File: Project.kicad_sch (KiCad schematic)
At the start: 76 parts, among them J1 Screw_Terminal_01x02, J2 Screw_Terminal_01x02, J3 Conn_01x04_Socket, Q1 BT136-500, SW1 PEC11H, SW2 PEC11H, U1 AMS1117-3.3, U2 ESP32-WROOM-32, U3 MOC3021M, U4 MCT2E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

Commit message: LED
LED has been connected
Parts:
- removed J3: Conn_01x04_Socket, Connector_PinHeader_1.27mm:PinHeader_1x04_P1.27mm_Vertical, symbol Connector:Conn_01x04_Socket
- added J3: Conn_01x03_Pin, Connector_PinHeader_1.00mm:PinHeader_1x03_P1.00mm_Horizontal, symbol Connector:Conn_01x03_Pin
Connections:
- net GND: now also J3.3 (Pin_3)
- net VCC33: now also R18.1; no longer R18.2
- net at DS1.16 (~{RES}): now also R18.2; no longer R18.1
- net UART_RX: now reaches U2.34 (RXD0/IO3)
- net UART_RX: now also J3.2 (Pin_2)
- net UART_TX: now reaches U2.35 (TXD0/IO1)
- net UART_TX: now also J3.1 (Pin_1)
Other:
- moved on the sheet: DS1

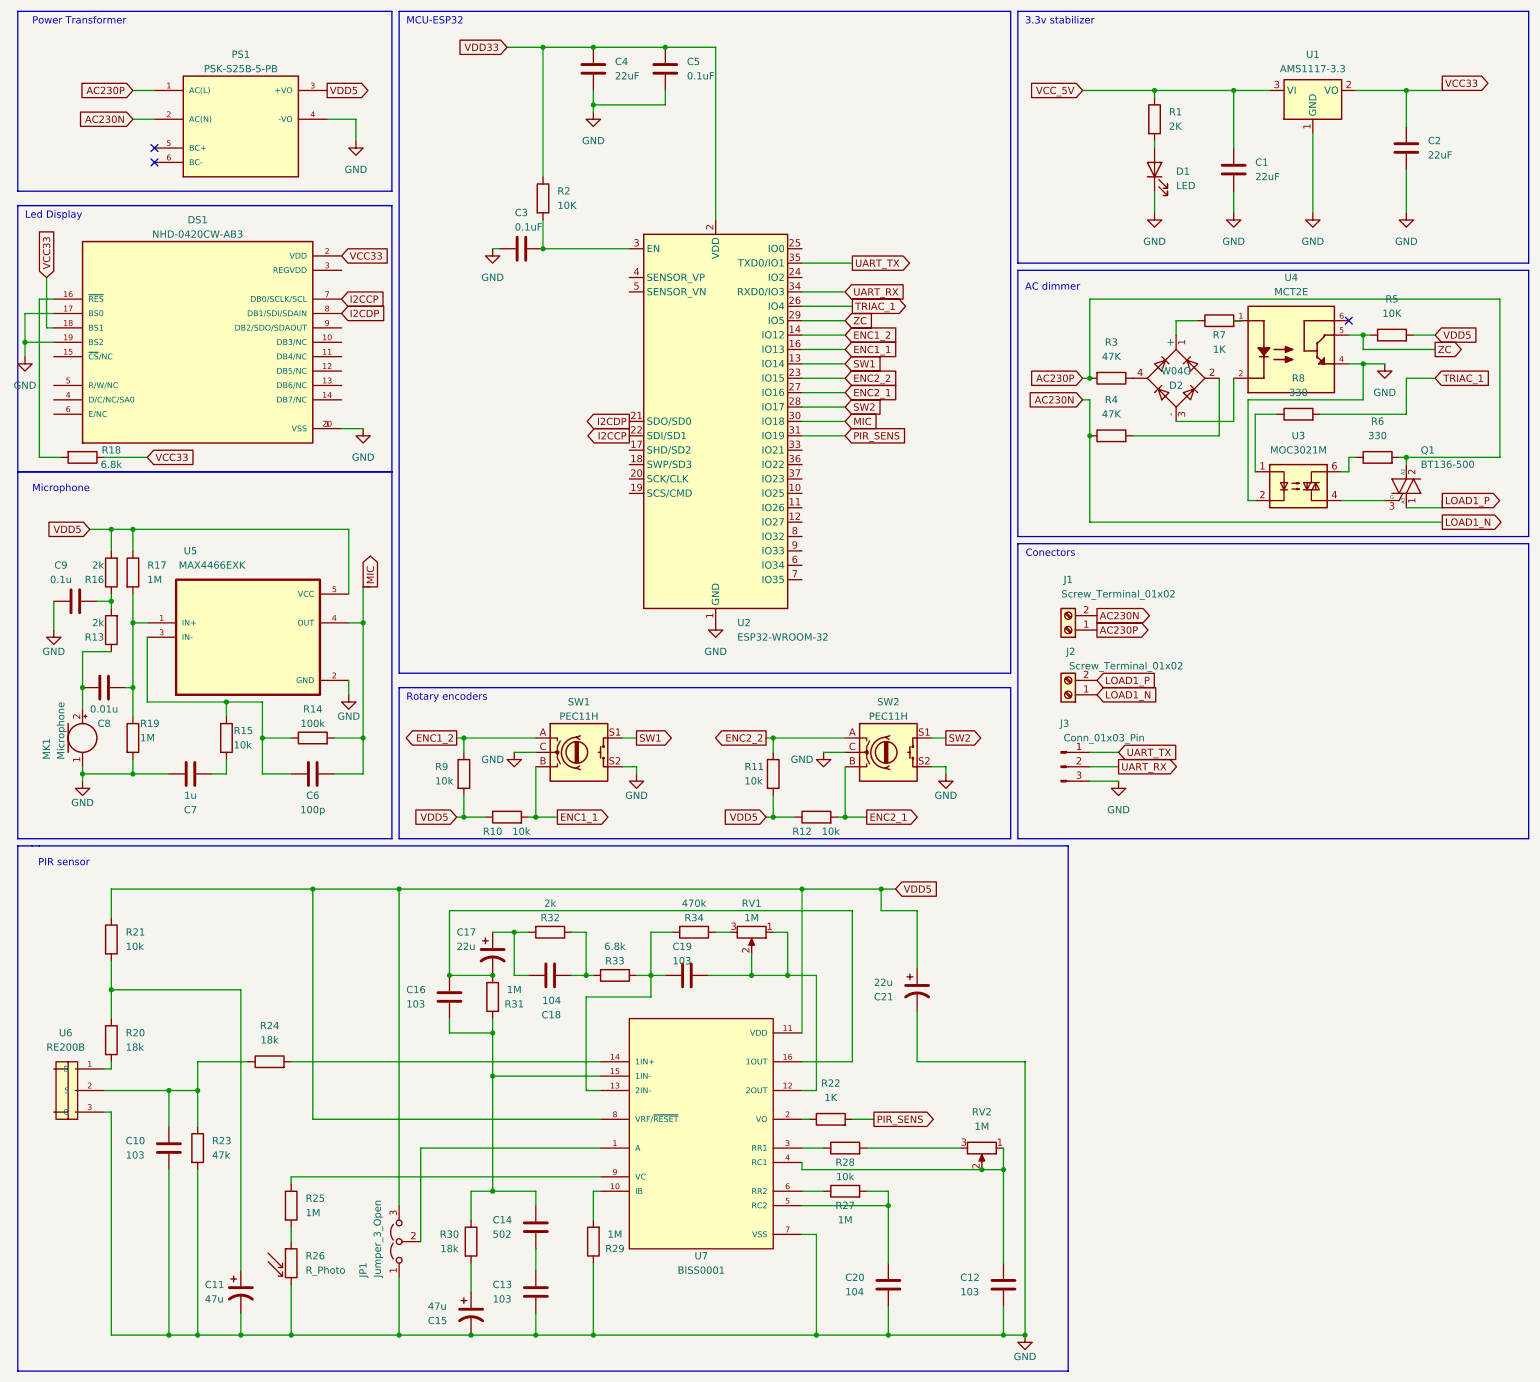
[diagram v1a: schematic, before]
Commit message: PCB components arranged + Power traces
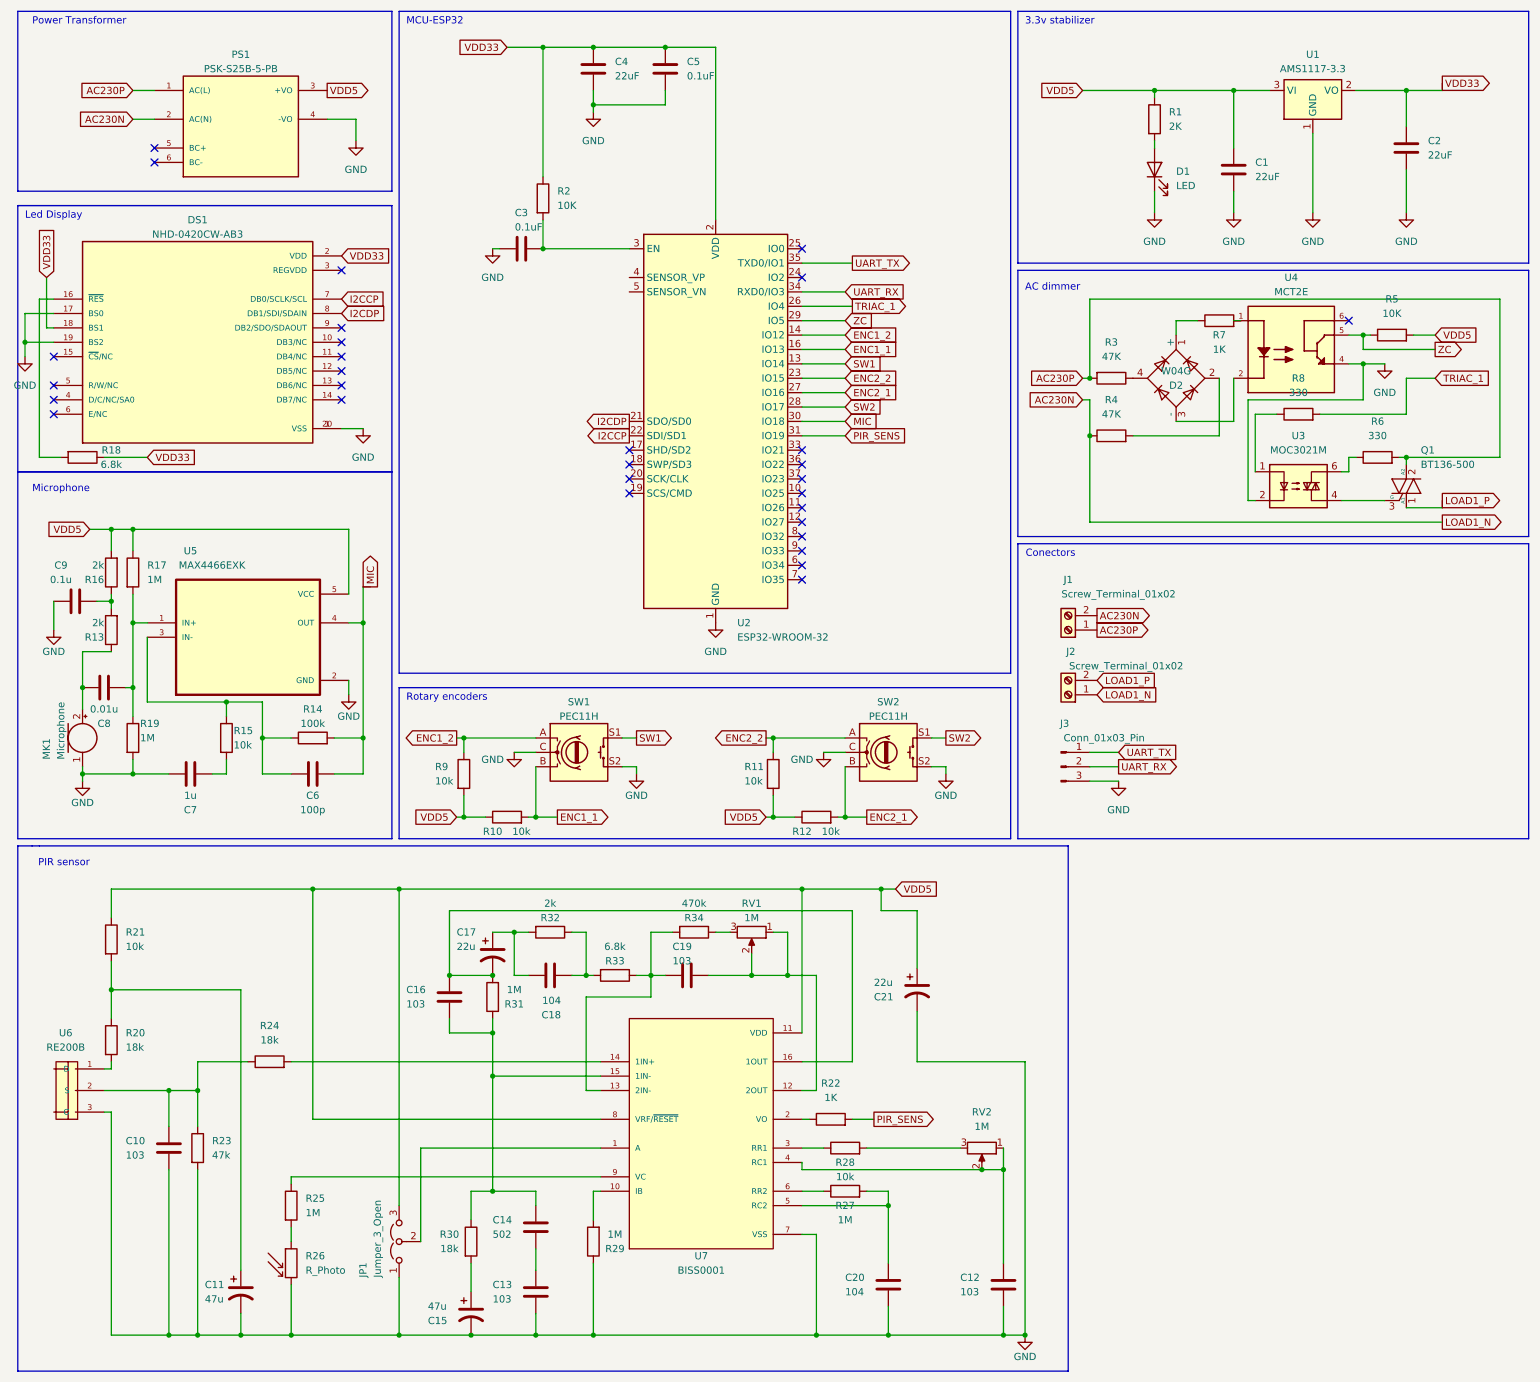
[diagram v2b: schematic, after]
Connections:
- net VCC33 is gone; now on net VDD33: C2.1, DS1.18 (BS1), DS1.2 (VDD), R18.1, U1.2 (VO)
- net VCC_5V is gone; now on net VDD5: C1.1, R1.1, U1.3 (VI)
- no-connect marks 3 -> 30
